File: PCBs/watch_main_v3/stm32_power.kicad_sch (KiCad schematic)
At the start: 23 parts

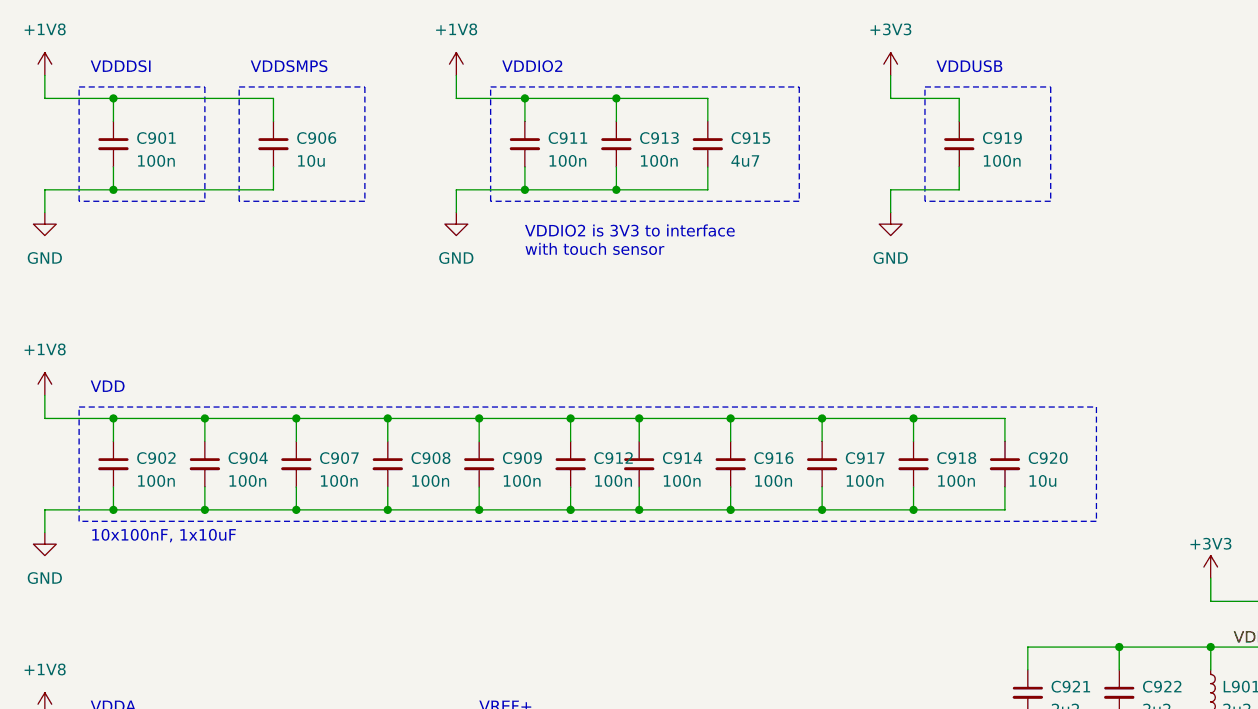
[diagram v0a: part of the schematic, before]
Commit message: watch_main_v3 removed unnecessary capacitors from schematic.
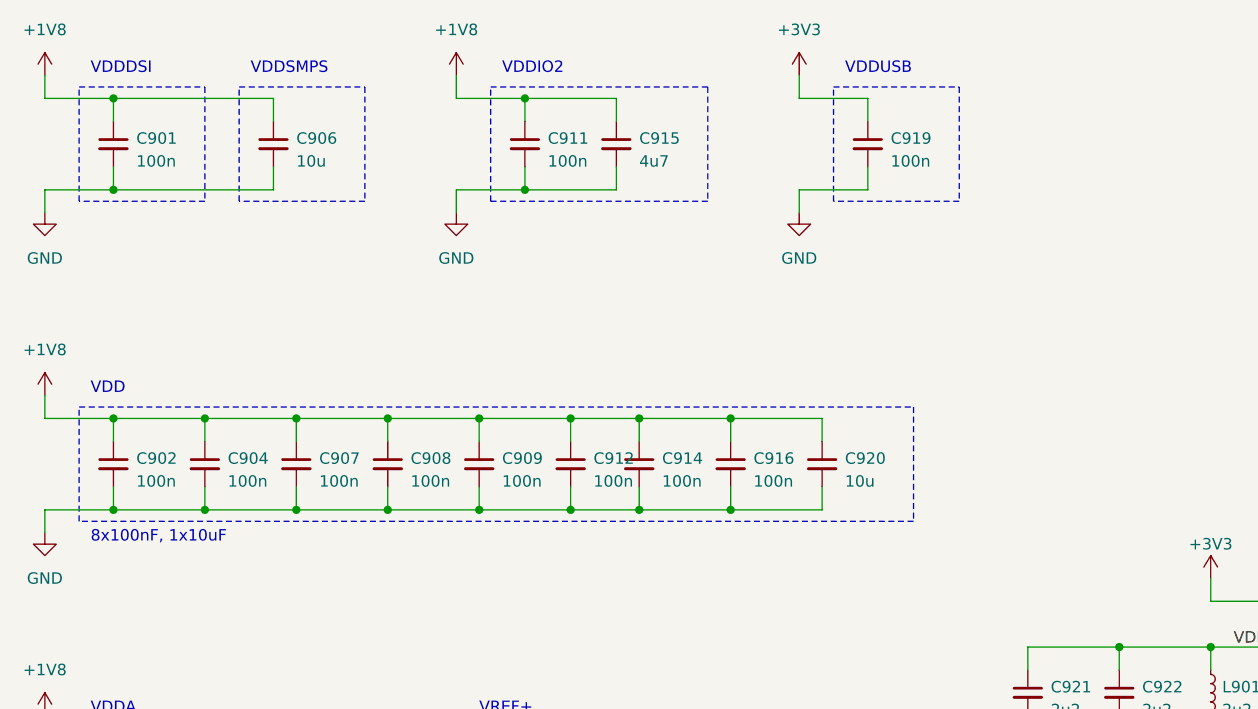
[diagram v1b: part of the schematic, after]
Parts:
- removed C913, C917, C918: 100n, Capacitor_SMD:C_0402_1005Metric, symbol Device:C_Small
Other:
- note added: "8x100nF, 1x10uF"
- note removed: "10x100nF, 1x10uF"
- note removed: "VDDIO2 is 3V3 to interface with touch sensor"
- moved on the sheet: C915, C919, C920

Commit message: PCB V3 progress
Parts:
- added C916: 100n, Capacitor_SMD:C_0201_0603Metric, symbol Device:C_Small
- added U801: STM32U5G9ZJJ6Q, watch_footprints:UFBGA144_STM, symbol STM32U5G9ZJJ6Q:STM32U5G9ZJJ6Q
- C901, C902, C903, C904, C905, C907, C908, C909, C911, C912, C914: footprint Capacitor_SMD:C_0402_1005Metric -> Capacitor_SMD:C_0201_0603Metric
- C910: value 100n -> 1u; footprint Capacitor_SMD:C_0402_1005Metric -> Capacitor_SMD:C_0201_0603Metric
- C915: renamed from C916; footprint Capacitor_SMD:C_0402_1005Metric -> Capacitor_SMD:C_0201_0603Metric
- C918: renamed from C919; footprint Capacitor_SMD:C_0402_1005Metric -> Capacitor_SMD:C_0201_0603Metric
- C919: renamed from C921; footprint Capacitor_SMD:C_0402_1005Metric -> Capacitor_SMD:C_0201_0603Metric
- C920: renamed from C922; footprint Capacitor_SMD:C_0402_1005Metric -> Capacitor_SMD:C_0201_0603Metric
- renumbered C915 to C913, C920 to C917
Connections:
- net +1V8: now also C916.1, U801.C2 (VBAT), U801.E10 (VDD), U801.E3 (VDDDSI), U801.E6 (VDDIO2), U801.E8 (VDD), U801.F5 (VDD), U801.G10 (VDD), U801.G8 (VDD), U801.H5 (VDD), U801.H7 (VDD), U801.J10 (VDD), U801.J4 (VDDA), U801.M8 (VDDSMPS)
- net +3V3: now also U801.D10 (VDDUSB)
- net GND: now also C916.2, U801.A1 (VSS), U801.A12 (VSS), U801.D1 (VSSDSI), U801.D5 (VSS), U801.D9 (VSS), U801.F10 (VSS), U801.F3 (VSSDSI), U801.F6 (VSS), U801.F7 (VSS), U801.G6 (VSS), U801.G7 (VSS), U801.H1 (VSSDSI), U801.H10 (VSS), U801.J3 (VSSA), U801.L8 (VSSSMPS), U801.M1 (VSS), U801.M12 (VSS)
- net VDD11: now also U801.D4 (VDD11), U801.G3 (VDD11DSI), U801.J9 (VDD11)
- net VLXSMPS: now also U801.M7 (VLXSMPS)
- net VREF+: now also U801.H3 (VREF+)
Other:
- note added: "VBAT"
- moved on the sheet: C901, C902, C903, C904, C905, C906, C907, C908, C909, C910, C911, C912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
